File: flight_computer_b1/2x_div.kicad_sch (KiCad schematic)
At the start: 2 parts

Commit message: flight computer: added pyro circuit and digikey part numbers
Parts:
- R51, R52: DIGIKEY PART N (none) -> YAG1237CT-ND
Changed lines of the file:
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@@
+			)
+		)
+		(property "DIGIKEY PART N" "YAG1237CT-ND"
+			(at 142.24 85.09 0)
+			(effects
+				(font
+					(size 1.27 1.27)
+				)
+				(hide yes)
 			)
 		)
@@
 			(at 142.24 97.79 0)
 			(effects
+				(font
+					(size 1.27 1.27)
+				)
+				(hide yes)
+			)
+		)
+		(property "DIGIKEY PART N" "YAG1237CT-ND"
+			(at 142.24 97.79 0)
+			(effects

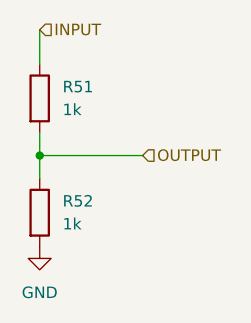
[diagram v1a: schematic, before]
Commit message: flight computer: routing updates
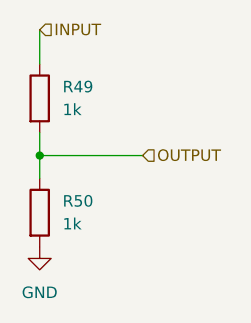
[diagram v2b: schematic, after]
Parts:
- renumbered R51 to R49, R52 to R50
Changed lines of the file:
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@@
 		(dnp no)
 		(fields_autoplaced yes)
-		(property "Reference" "#PWR065"
+		(property "Reference" "#PWR067"
 			(at 142.24 107.95 0)
 			(effects
@@
 			(project "flight_computer"
 				(path "/b71a7b79-cdb5-4e38-a72c-0daaa3474f05/4025abfc-a6bf-4171-88b8-c419fa084ae6"
-					(reference "#PWR065")
+					(reference "#PWR067")
 					(unit 1)
 				)
@@
 		(dnp no)
 		(fields_autoplaced yes)
-		(property "Reference" "R51"
+		(property "Reference" "R49"
 			(at 144.78 83.8199 0)
 			(effects
@@
 			(project "flight_computer"
 				(path "/b71a7b79-cdb5-4e38-a72c-0daaa3474f05/4025abfc-a6bf-4171-88b8-c419fa084ae6"
-					(reference "R51")
+					(reference "R49")
 					(unit 1)
 				)
@@
 		(dnp no)
 		(fields_autoplaced yes)
-		(property "Reference" "R52"
+		(property "Reference" "R50"
 			(at 144.78 96.5199 0)
 			(effects
@@
 			(project "flight_computer"
 				(path "/b71a7b79-cdb5-4e38-a72c-0daaa3474f05/4025abfc-a6bf-4171-88b8-c419fa084ae6"
-					(reference "R52")
+					(reference "R50")
 					(unit 1)
 				)
